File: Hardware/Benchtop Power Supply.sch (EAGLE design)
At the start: 24 parts, among them J1 ATX24RH

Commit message: Updating to new binding post footprint
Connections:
- net -12V_P: now also S8.P$1
- net 12V_P: now also S6.P$1
- net 3.3V_P: now also S2.P$1
- net 5V_P: now also S4.P$1
- net GND: now also S1.P$1, S3.P$1, S5.P$1, S7.P$1
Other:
- moved on the sheet: F1, LED1, R1
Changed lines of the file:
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@@
 <instance part="JP5" gate="G$1" x="246.38" y="25.4"/>
 <instance part="J1" gate="G$1" x="121.92" y="104.14"/>
-<instance part="GND1" gate="1" x="104.14" y="78.74"/>
+<instance part="GND1" gate="1" x="96.52" y="78.74"/>
 <instance part="GND2" gate="1" x="149.86" y="78.74"/>
-<instance part="F1" gate="G$1" x="76.2" y="121.92"/>
+<instance part="F1" gate="G$1" x="48.26" y="121.92"/>
 <instance part="F2" gate="G$1" x="165.1" y="121.92"/>
 <instance part="F3" gate="G$1" x="165.1" y="104.14"/>
 <instance part="F4" gate="G$1" x="165.1" y="96.52"/>
-<instance part="R1" gate="G$1" x="91.44" y="114.3" rot="R90"/>
-<instance part="LED1" gate="G$1" x="91.44" y="104.14"/>
-<instance part="GND3" gate="1" x="91.44" y="93.98"/>
-<instance part="S1" gate="G$1" x="208.28" y="121.92"/>
-<instance part="S2" gate="G$1" x="213.36" y="121.92"/>
-<instance part="S3" gate="G$1" x="208.28" y="104.14"/>
-<instance part="S4" gate="G$1" x="213.36" y="104.14"/>
-<instance part="S5" gate="G$1" x="208.28" y="96.52"/>
-<instance part="S6" gate="G$1" x="213.36" y="96.52"/>
-<instance part="S7" gate="G$1" x="43.18" y="121.92"/>
-<instance part="S8" gate="G$1" x="38.1" y="121.92"/>
+<instance part="R1" gate="G$1" x="66.04" y="114.3" rot="R90"/>
+<instance part="LED1" gate="G$1" x="66.04" y="104.14"/>
+<instance part="GND3" gate="1" x="66.04" y="78.74"/>
+<instance part="S1" gate="G$1" x="93.98" y="91.44" rot="R180"/>
+<instance part="S2" gate="G$1" x="193.04" y="121.92"/>
+<instance part="S3" gate="G$1" x="93.98" y="86.36" rot="R180"/>
+<instance part="S4" gate="G$1" x="33.02" y="121.92" rot="R180"/>
+<instance part="S5" gate="G$1" x="93.98" y="96.52" rot="R180"/>
+<instance part="S6" gate="G$1" x="193.04" y="104.14"/>
+<instance part="S7" gate="G$1" x="93.98" y="99.06" rot="R180"/>
+<instance part="S8" gate="G$1" x="193.04" y="96.52"/>
 <instance part="S9" gate="1" x="142.24" y="91.44"/>
 <instance part="U$1" gate="G$1" x="148.59" y="7.112"/>
@@
 <net name="GND" class="0">
 <segment>
-<wire x1="106.68" y1="83.82" x2="104.14" y2="83.82" width="0.1524" layer="91"/>
-<wire x1="104.14" y1="83.82" x2="104.14" y2="81.28" width="0.1524" layer="91"/>
-<wire x1="106.68" y1="86.36" x2="104.14" y2="86.36" width="0.1524" layer="91"/>
-<wire x1="104.14" y1="86.36" x2="104.14" y2="83.82" width="0.1524" layer="91"/>
-<wire x1="106.68" y1="88.9" x2="104.14" y2="88.9" width="0.1524" layer="91"/>
-<wire x1="104.14" y1="88.9" x2="104.14" y2="86.36" width="0.1524" layer="91"/>
-<wire x1="106.68" y1="91.44" x2="104.14" y2="91.44" width="0.1524" layer="91"/>
-<wire x1="104.14" y1="91.44" x2="104.14" y2="88.9" width="0.1524" layer="91"/>
-<wire x1="106.68" y1="93.98" x2="104.14" y2="93.98" width="0.1524" layer="91"/>
-<wire x1="104.14" y1="93.98" x2="104.14" y2="91.44" width="0.1524" layer="91"/>
-<wire x1="106.68" y1="96.52" x2="104.14" y2="96.52" width="0.1524" layer="91"/>
-<wire x1="104.14" y1="96.52" x2="104.14" y2="93.98" width="0.1524" layer="91"/>
-<wire x1="106.68" y1="99.06" x2="104.14" y2="99.06" width="0.1524" layer="91"/>
-<wire x1="104.14" y1="99.06" x2="104.14" y2="96.52" width="0.1524" layer="91"/>
-<wire x1="106.68" y1="101.6" x2="104.14" y2="101.6" width="0.1524" layer="91"/>
-<wire x1="104.14" y1="101.6" x2="104.14" y2="99.06" width="0.1524" layer="91"/>
-<junction x="104.14" y="83.82"/>
-<junction x="104.14" y="86.36"/>
-<junction x="104.14" y="88.9"/>
-<junction x="104.14" y="91.44"/>
-<junction x="104.14" y="93.98"/>
-<junction x="104.14" y="96.52"/>
-<junction x="104.14" y="99.06"/>
+<wire x1="106.68" y1="83.82" x2="96.52" y2="83.82" width="0.1524" layer="91"/>
+<wire x1="96.52" y1="83.82" x2="96.52" y2="81.28" width="0.1524" layer="91"/>
+<wire x1="106.68" y1="86.36" x2="96.52" y2="86.36" width="0.1524" layer="91"/>
+<wire x1="96.52" y1="86.36" x2="96.52" y2="83.82" width="0.1524" layer="91"/>
+<wire x1="106.68" y1="88.9" x2="96.52" y2="88.9" width="0.1524" layer="91"/>
+<wire x1="96.52" y1="88.9" x2="96.52" y2="86.36" width="0.1524" layer="91"/>
+<wire x1="106.68" y1="91.44" x2="96.52" y2="91.44" width="0.1524" layer="91"/>
+<wire x1="96.52" y1="91.44" x2="96.52" y2="88.9" width="0.1524" layer="91"/>
+<wire x1="106.68" y1="93.98" x2="96.52" y2="93.98" width="0.1524" layer="91"/>
+<wire x1="96.52" y1="93.98" x2="96.52" y2="91.44" width="0.1524" layer="91"/>
+<wire x1="106.68" y1="96.52" x2="96.52" y2="96.52" width="0.1524" layer="91"/>
+<wire x1="96.52" y1="96.52" x2="96.52" y2="93.98" width="0.1524" layer="91"/>
+<wire x1="106.68" y1="99.06" x2="96.52" y2="99.06" width="0.1524" layer="91"/>
+<wire x1="96.52" y1="99.06" x2="96.52" y2="96.52" width="0.1524" layer="91"/>
+<wire x1="106.68" y1="101.6" x2="96.52" y2="101.6" width="0.1524" layer="91"/>
+<wire x1="96.52" y1="101.6" x2="96.52" y2="99.06" width="0.1524" layer="91"/>
+<junction x="96.52" y="83.82"/>
+<junction x="96.52" y="86.36"/>
+<junction x="96.52" y="88.9"/>
+<junction x="96.52" y="91.44"/>
+<junction x="96.52" y="93.98"/>
+<junction x="96.52" y="96.52"/>
+<junction x="96.52" y="99.06"/>
 <pinref part="J1" gate="G$1" pin="GND@0"/>
 <pinref part="GND1" gate="1" pin="GND"/>
@@
 <pinref part="J1" gate="G$1" pin="GND@6"/>
 <pinref part="J1" gate="G$1" pin="GND@7"/>
+<pinref part="S7" gate="G$1" pin="P$1"/>
+<pinref part="S1" gate="G$1" pin="P$1"/>
+<pinref part="S3" gate="G$1" pin="P$1"/>
+<pinref part="S5" gate="G$1" pin="P$1"/>
 </segment>
 <segment>
-<wire x1="91.44" y1="96.52" x2="91.44" y2="99.06" width="0.1524" layer="91"/>
+<wire x1="66.04" y1="81.28" x2="66.04" y2="99.06" width="0.1524" layer="91"/>
 <pinref part="GND3" gate="1" pin="GND"/>
 <pinref part="LED1" gate="G$1" pin="C"/>
@@
 <segment>
 <wire x1="106.68" y1="121.92" x2="104.14" y2="121.92" width="0.1524" layer="91"/>
-<wire x1="104.14" y1="121.92" x2="91.44" y2="121.92" width="0.1524" layer="91"/>
+<wire x1="104.14" y1="121.92" x2="66.04" y2="121.92" width="0.1524" layer="91"/>
 <wire x1="106.68" y1="119.38" x2="104.14" y2="119.38" width="0.1524" layer="91"/>
 <wire x1="104.14" y1="119.38" x2="104.14" y2="121.92" width="0.1524" layer="91"/>
@@
 <wire x1="106.68" y1="111.76" x2="104.14" y2="111.76" width="0.1524" layer="91"/>
 <wire x1="104.14" y1="111.76" x2="104.14" y2="114.3" width="0.1524" layer="91"/>
-<wire x1="86.36" y1="121.92" x2="91.44" y2="121.92" width="0.1524" layer="91"/>
-<wire x1="91.44" y1="119.38" x2="91.44" y2="121.92" width="0.1524" layer="91"/>
+<wire x1="58.42" y1="121.92" x2="66.04" y2="121.92" width="0.1524" layer="91"/>
+<wire x1="66.04" y1="119.38" x2="66.04" y2="121.92" width="0.1524" layer="91"/>
 <junction x="104.14" y="121.92"/>
 <junction x="104.14" y="119.38"/>
 <junction x="104.14" y="116.84"/>
 <junction x="104.14" y="114.3"/>
-<junction x="91.44" y="121.92"/>
-<label x="91.44" y="121.92" size="1.778" layer="95"/>
+<junction x="66.04" y="121.92"/>
+<label x="68.58" y="121.92" size="1.778" layer="95"/>
 <pinref part="J1" gate="G$1" pin="5V@4"/>
 <pinref part="J1" gate="G$1" pin="5V@3"/>
@@
 <net name="5V_P" class="0">
 <segment>
-<wire x1="66.04" y1="121.92" x2="58.42" y2="121.92" width="0.1524" layer="91"/>
+<wire x1="38.1" y1="121.92" x2="35.56" y2="121.92" width="0.1524" layer="91"/>
 <pinref part="F1" gate="G$1" pin="1"/>
-<label x="58.42" y="121.92" size="1.778" layer="95" rot="R180" xref="yes"/>
+<pinref part="S4" gate="G$1" pin="P$1"/>
 </segment>
 </net>
@@
 <wire x1="175.26" y1="121.92" x2="190.5" y2="121.92" width="0.1524" layer="91"/>
 <pinref part="F2" gate="G$1" pin="2"/>
-<label x="190.5" y="121.92" size="1.778" layer="95" xref="yes"/>
+<pinref part="S2" gate="G$1" pin="P$1"/>
 </segment>
 </net>
@@
 <wire x1="175.26" y1="104.14" x2="190.5" y2="104.14" width="0.1524" layer="91"/>
 <pinref part="F3" gate="G$1" pin="2"/>
-<label x="190.5" y="104.14" size="1.778" layer="95" xref="yes"/>
+<pinref part="S6" gate="G$1" pin="P$1"/>
 </segment>
 </net>
@@
 <wire x1="175.26" y1="96.52" x2="190.5" y2="96.52" width="0.1524" layer="91"/>
 <pinref part="F4" gate="G$1" pin="2"/>
-<label x="190.5" y="96.52" size="1.778" layer="95" xref="yes"/>
+<pinref part="S8" gate="G$1" pin="P$1"/>
 </segment>
 </net>
 <net name="N$1" class="0">
 <segment>
-<wire x1="91.44" y1="106.68" x2="91.44" y2="109.22" width="0.1524" layer="91"/>
+<wire x1="66.04" y1="106.68" x2="66.04" y2="109.22" width="0.1524" layer="91"/>
 <pinref part="LED1" gate="G$1" pin="A"/>
 <pinref part="R1" gate="G$1" pin="1"/>

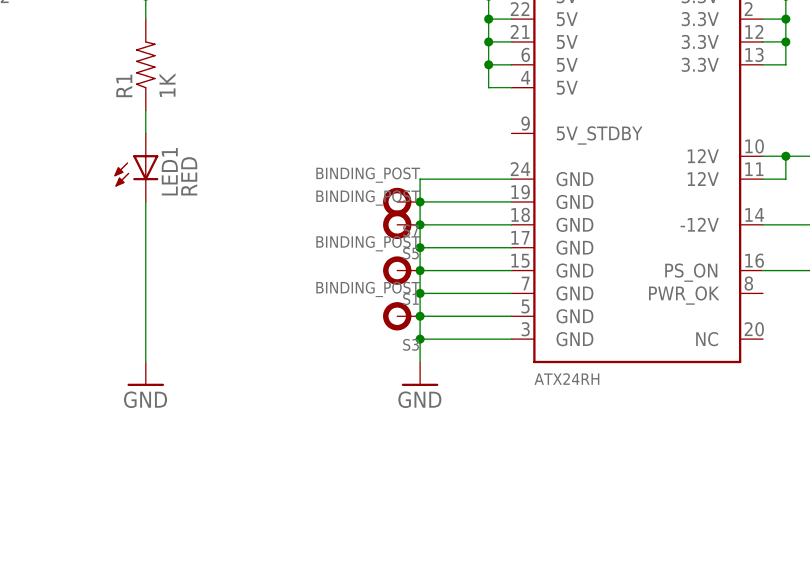
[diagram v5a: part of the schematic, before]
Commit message: Fixing review commentaries
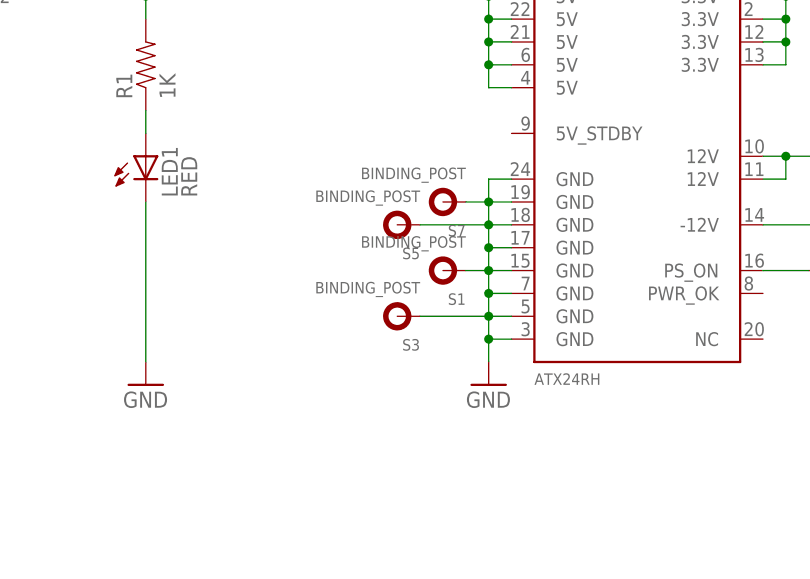
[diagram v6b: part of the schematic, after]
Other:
- moved on the sheet: S1, S7
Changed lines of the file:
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@@
 <instance part="JP5" gate="G$1" x="246.38" y="25.4"/>
 <instance part="J1" gate="G$1" x="121.92" y="104.14"/>
-<instance part="GND1" gate="1" x="96.52" y="78.74"/>
+<instance part="GND1" gate="1" x="104.14" y="78.74"/>
 <instance part="GND2" gate="1" x="149.86" y="78.74"/>
 <instance part="F1" gate="G$1" x="48.26" y="121.92"/>
@@
 <instance part="LED1" gate="G$1" x="66.04" y="104.14"/>
 <instance part="GND3" gate="1" x="66.04" y="78.74"/>
-<instance part="S1" gate="G$1" x="93.98" y="91.44" rot="R180"/>
+<instance part="S1" gate="G$1" x="99.06" y="91.44" rot="R180"/>
 <instance part="S2" gate="G$1" x="193.04" y="121.92"/>
 <instance part="S3" gate="G$1" x="93.98" y="86.36" rot="R180"/>
@@
 <instance part="S5" gate="G$1" x="93.98" y="96.52" rot="R180"/>
 <instance part="S6" gate="G$1" x="193.04" y="104.14"/>
-<instance part="S7" gate="G$1" x="93.98" y="99.06" rot="R180"/>
+<instance part="S7" gate="G$1" x="99.06" y="99.06" rot="R180"/>
 <instance part="S8" gate="G$1" x="193.04" y="96.52"/>
 <instance part="S9" gate="1" x="142.24" y="91.44"/>
@@
 <net name="GND" class="0">
 <segment>
-<wire x1="106.68" y1="83.82" x2="96.52" y2="83.82" width="0.1524" layer="91"/>
-<wire x1="96.52" y1="83.82" x2="96.52" y2="81.28" width="0.1524" layer="91"/>
-<wire x1="106.68" y1="86.36" x2="96.52" y2="86.36" width="0.1524" layer="91"/>
-<wire x1="96.52" y1="86.36" x2="96.52" y2="83.82" width="0.1524" layer="91"/>
-<wire x1="106.68" y1="88.9" x2="96.52" y2="88.9" width="0.1524" layer="91"/>
-<wire x1="96.52" y1="88.9" x2="96.52" y2="86.36" width="0.1524" layer="91"/>
-<wire x1="106.68" y1="91.44" x2="96.52" y2="91.44" width="0.1524" layer="91"/>
-<wire x1="96.52" y1="91.44" x2="96.52" y2="88.9" width="0.1524" layer="91"/>
-<wire x1="106.68" y1="93.98" x2="96.52" y2="93.98" width="0.1524" layer="91"/>
-<wire x1="96.52" y1="93.98" x2="96.52" y2="91.44" width="0.1524" layer="91"/>
-<wire x1="106.68" y1="96.52" x2="96.52" y2="96.52" width="0.1524" layer="91"/>
-<wire x1="96.52" y1="96.52" x2="96.52" y2="93.98" width="0.1524" layer="91"/>
-<wire x1="106.68" y1="99.06" x2="96.52" y2="99.06" width="0.1524" layer="91"/>
-<wire x1="96.52" y1="99.06" x2="96.52" y2="96.52" width="0.1524" layer="91"/>
-<wire x1="106.68" y1="101.6" x2="96.52" y2="101.6" width="0.1524" layer="91"/>
-<wire x1="96.52" y1="101.6" x2="96.52" y2="99.06" width="0.1524" layer="91"/>
-<junction x="96.52" y="83.82"/>
-<junction x="96.52" y="86.36"/>
-<junction x="96.52" y="88.9"/>
-<junction x="96.52" y="91.44"/>
-<junction x="96.52" y="93.98"/>
-<junction x="96.52" y="96.52"/>
-<junction x="96.52" y="99.06"/>
 <pinref part="J1" gate="G$1" pin="GND@0"/>
+<wire x1="106.68" y1="83.82" x2="104.14" y2="83.82" width="0.1524" layer="91"/>
+<wire x1="104.14" y1="83.82" x2="104.14" y2="81.28" width="0.1524" layer="91"/>
 <pinref part="GND1" gate="1" pin="GND"/>
+<wire x1="106.68" y1="86.36" x2="104.14" y2="86.36" width="0.1524" layer="91"/>
+<wire x1="104.14" y1="86.36" x2="96.52" y2="86.36" width="0.1524" layer="91"/>
+<wire x1="106.68" y1="88.9" x2="104.14" y2="88.9" width="0.1524" layer="91"/>
 <pinref part="J1" gate="G$1" pin="GND@1"/>
 <pinref part="J1" gate="G$1" pin="GND@2"/>
+<pinref part="S3" gate="G$1" pin="P$1"/>
+<pinref part="J1" gate="G$1" pin="GND@7"/>
+<wire x1="106.68" y1="101.6" x2="104.14" y2="101.6" width="0.1524" layer="91"/>
+<pinref part="J1" gate="G$1" pin="GND@6"/>
+<wire x1="106.68" y1="99.06" x2="104.14" y2="99.06" width="0.1524" layer="91"/>
+<pinref part="S7" gate="G$1" pin="P$1"/>
+<wire x1="104.14" y1="99.06" x2="101.6" y2="99.06" width="0.1524" layer="91"/>
+<wire x1="104.14" y1="101.6" x2="104.14" y2="99.06" width="0.1524" layer="91"/>
+<pinref part="J1" gate="G$1" pin="GND@5"/>
+<wire x1="106.68" y1="96.52" x2="104.14" y2="96.52" width="0.1524" layer="91"/>
+<pinref part="S5" gate="G$1" pin="P$1"/>
+<wire x1="104.14" y1="96.52" x2="96.52" y2="96.52" width="0.1524" layer="91"/>
+<wire x1="104.14" y1="99.06" x2="104.14" y2="96.52" width="0.1524" layer="91"/>
+<pinref part="J1" gate="G$1" pin="GND@4"/>
+<wire x1="106.68" y1="93.98" x2="104.14" y2="93.98" width="0.1524" layer="91"/>
+<wire x1="104.14" y1="96.52" x2="104.14" y2="93.98" width="0.1524" layer="91"/>
 <pinref part="J1" gate="G$1" pin="GND@3"/>
-<pinref part="J1" gate="G$1" pin="GND@4"/>
-<pinref part="J1" gate="G$1" pin="GND@5"/>
-<pinref part="J1" gate="G$1" pin="GND@6"/>
-<pinref part="J1" gate="G$1" pin="GND@7"/>
-<pinref part="S7" gate="G$1" pin="P$1"/>
+<wire x1="106.68" y1="91.44" x2="104.14" y2="91.44" width="0.1524" layer="91"/>
 <pinref part="S1" gate="G$1" pin="P$1"/>
-<pinref part="S3" gate="G$1" pin="P$1"/>
-<pinref part="S5" gate="G$1" pin="P$1"/>
+<wire x1="104.14" y1="91.44" x2="101.6" y2="91.44" width="0.1524" layer="91"/>
+<wire x1="104.14" y1="93.98" x2="104.14" y2="91.44" width="0.1524" layer="91"/>
+<wire x1="104.14" y1="91.44" x2="104.14" y2="88.9" width="0.1524" layer="91"/>
+<wire x1="104.14" y1="88.9" x2="104.14" y2="86.36" width="0.1524" layer="91"/>
+<wire x1="104.14" y1="86.36" x2="104.14" y2="83.82" width="0.1524" layer="91"/>
+<junction x="104.14" y="96.52"/>
+<junction x="104.14" y="99.06"/>
+<junction x="104.14" y="93.98"/>
+<junction x="104.14" y="91.44"/>
+<junction x="104.14" y="88.9"/>
+<junction x="104.14" y="86.36"/>
+<junction x="104.14" y="83.82"/>
 </segment>
 <segment>
